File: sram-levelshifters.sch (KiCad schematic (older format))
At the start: 16 parts, among them U10 TXB0108-PW, U11 ISSI61WV5128BL, U12 ISSI61WV5128BL, U13 ISSI61WV5128BL, U14 ISSI61WV5128BL, U2 74HC04, U4 TXB0108-PW, U5 TXB0108-PW, U6 TXB0108-PW, U7 74HC04, U8 TXB0108-PW, U9 74HC04

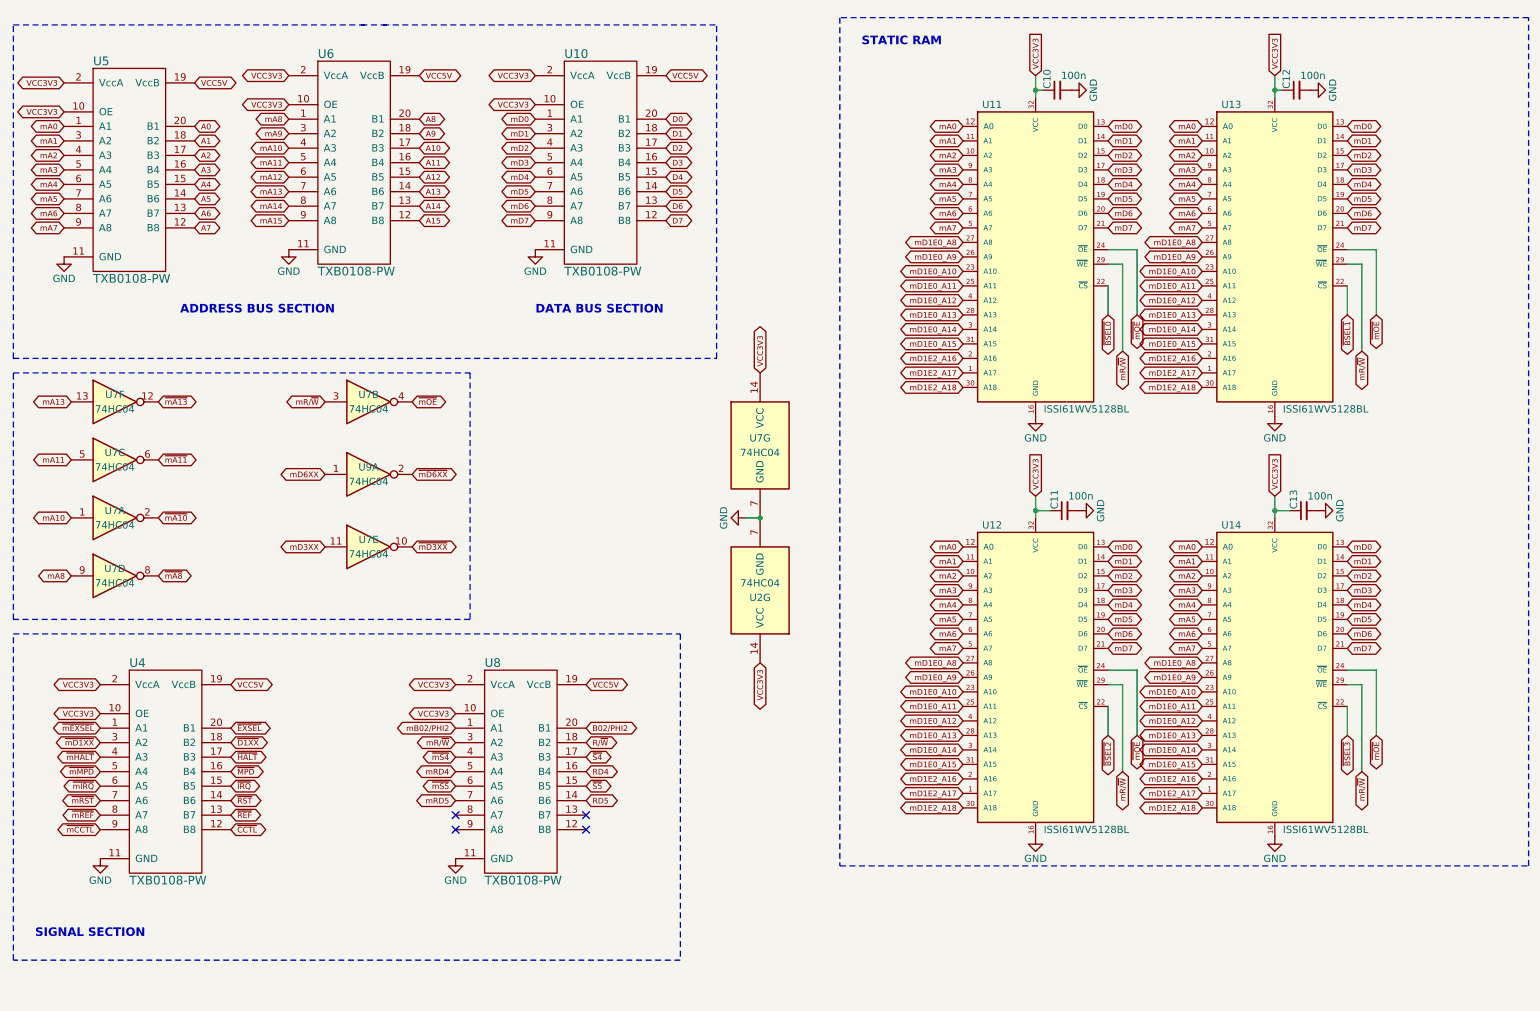
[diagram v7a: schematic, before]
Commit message: Heavily modified. Now it sports a 1024/2048k MIO Ram Expansion and a UNO Cart
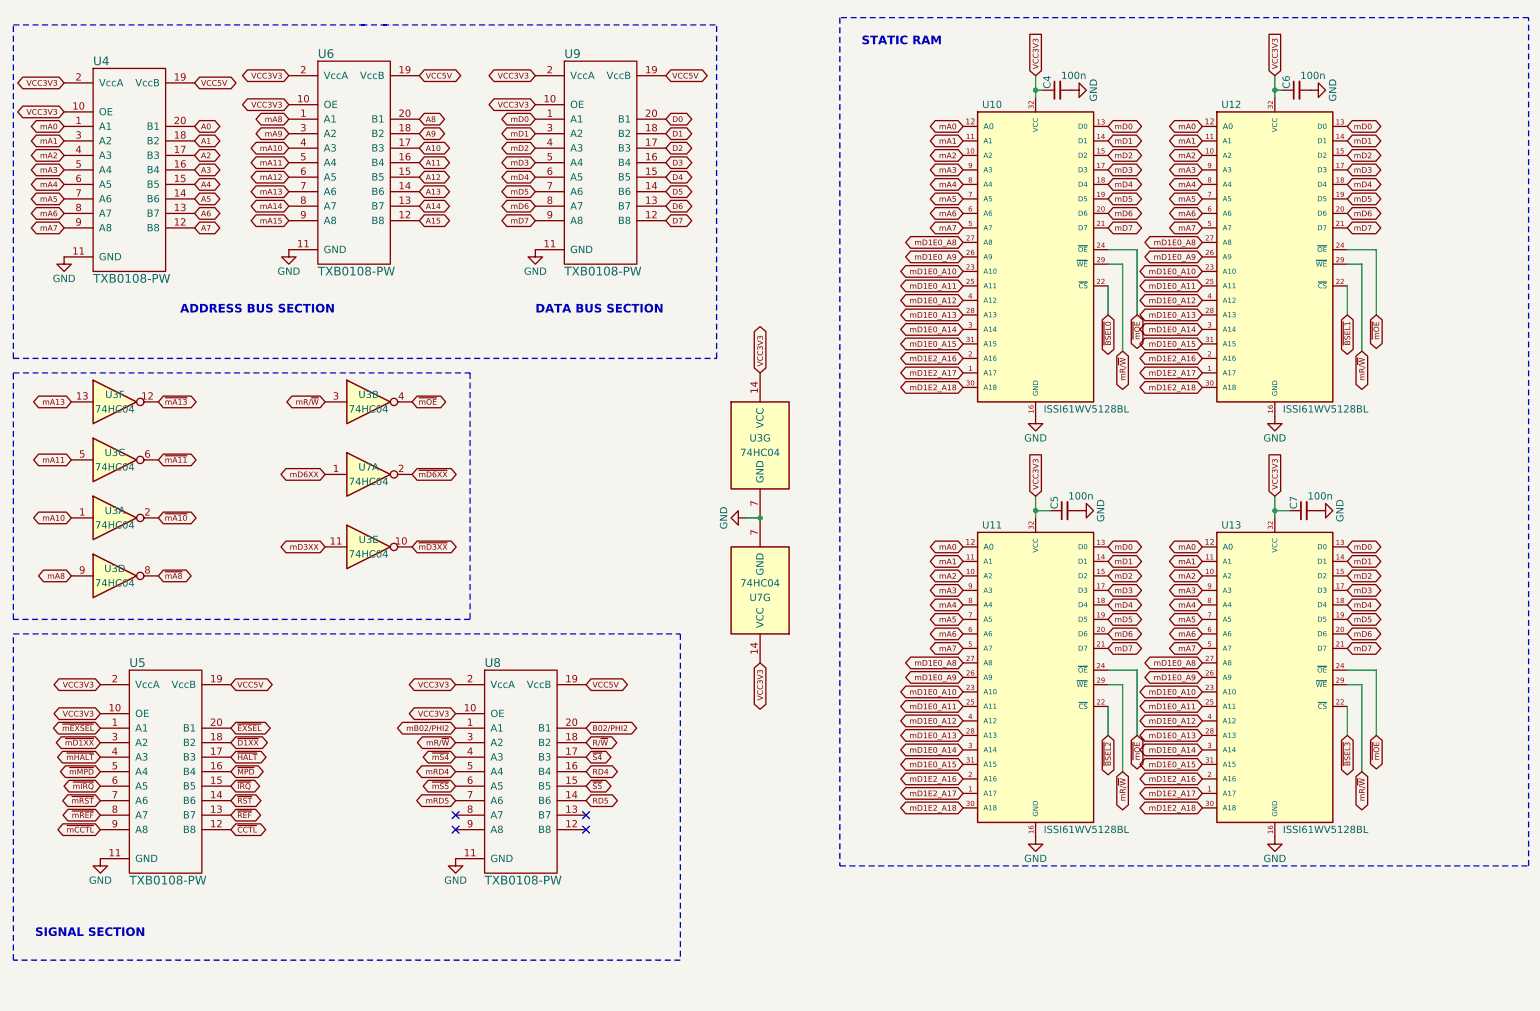
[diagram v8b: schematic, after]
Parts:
- renumbered C10 to C4, C11 to C5, C12 to C6, C13 to C7, U11 to U10, U12 to U11, U13 to U12, U14 to U13, U7 to U3, U5 to U4, U4 to U5, U2 to U7, U9 to U7, U10 to U9
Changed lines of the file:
@@
 $EndDescr
 $Comp
-L ISSI61WV5128BL U11
+L ISSI61WV5128BL U10
 U 1 1 5C2B9006
 P 7650 2250
-F 0 "U11" H 7350 3300 50  0000 C CNN
+F 0 "U10" H 7350 3300 50  0000 C CNN
 F 1 "ISSI61WV5128BL" H 8000 1200 50  0000 C CNN
 F 2 "RetroBitLab:SOP-32L-20.5x11.30-1.27mm" H 7650 2250 50  0001 C CIN
@@
 	7650 1000 7650 1150
 $Comp
-L C_Small C10
+L C_Small C4
 U 1 1 5C2BF542
 P 7800 1100
-F 0 "C10" H 7810 1170 50  0000 L CNN
+F 0 "C4" H 7810 1170 50  0000 L CNN
 F 1 "100n" V 7900 900 50  0000 L CNN
 F 2 "Capacitors_SMD:C_1206_HandSoldering" H 7800 1100 50  0001 C CNN
@@
 $EndComp
 $Comp
-L TXB0108-PW U5
+L TXB0108-PW U4
 U 1 1 5C2BF846
 P 1350 1650
-F 0 "U5" H 1150 2400 60  0000 L CNN
+F 0 "U4" H 1150 2400 60  0000 L CNN
 F 1 "TXB0108-PW" H 1150 900 60  0000 L CNN
 F 2 "Housings_SSOP:SSOP-20_4.4x6.5mm_Pitch0.65mm" H 1150 1600 60  0001 C CNN
@@
 $EndComp
 $Comp
-L TXB0108-PW U4
+L TXB0108-PW U5
 U 1 1 5C2BF9CC
 P 1600 5800
-F 0 "U4" H 1400 6550 60  0000 L CNN
+F 0 "U5" H 1400 6550 60  0000 L CNN
 F 1 "TXB0108-PW" H 1400 5050 60  0000 L CNN
 F 2 "Housings_SSOP:SSOP-20_4.4x6.5mm_Pitch0.65mm" H 1400 5750 60  0001 C CNN
@@
 $EndComp
 $Comp
-L TXB0108-PW U10
+L TXB0108-PW U9
 U 1 1 5C2BFAD5
 P 4600 1600
-F 0 "U10" H 4400 2350 60  0000 L CNN
+F 0 "U9" H 4400 2350 60  0000 L CNN
 F 1 "TXB0108-PW" H 4400 850 60  0000 L CNN
 F 2 "Housings_SSOP:SSOP-20_4.4x6.5mm_Pitch0.65mm" H 4400 1550 60  0001 C CNN
@@
 mD7
 $Comp
-L ISSI61WV5128BL U13
+L ISSI61WV5128BL U12
 U 1 1 5C2DCB84
 P 9300 2250
-F 0 "U13" H 9000 3300 50  0000 C CNN
+F 0 "U12" H 9000 3300 50  0000 C CNN
 F 1 "ISSI61WV5128BL" H 9650 1200 50  0000 C CNN
 F 2 "RetroBitLab:SOP-32L-20.5x11.30-1.27mm" H 9300 2250 50  0001 C CIN
@@
 	9300 1000 9300 1150
 $Comp
-L C_Small C12
+L C_Small C6
 U 1 1 5C2DCB9F
 P 9450 1100
-F 0 "C12" H 9460 1170 50  0000 L CNN
+F 0 "C6" H 9460 1170 50  0000 L CNN
 F 1 "100n" V 9550 900 50  0000 L CNN
 F 2 "Capacitors_SMD:C_1206_HandSoldering" H 9450 1100 50  0001 C CNN
@@
 mD7
 $Comp
-L ISSI61WV5128BL U12
+L ISSI61WV5128BL U11
 U 1 1 5C2DCEF9
 P 7650 5150
-F 0 "U12" H 7350 6200 50  0000 C CNN
+F 0 "U11" H 7350 6200 50  0000 C CNN
 F 1 "ISSI61WV5128BL" H 8000 4100 50  0000 C CNN
 F 2 "RetroBitLab:SOP-32L-20.5x11.30-1.27mm" H 7650 5150 50  0001 C CIN
@@
 	7650 3900 7650 4050
 $Comp
-L C_Small C11
+L C_Small C5
 U 1 1 5C2DCF14
 P 7850 4000
-F 0 "C11" H 7860 4070 50  0000 L CNN
+F 0 "C5" H 7860 4070 50  0000 L CNN
 F 1 "100n" V 7950 3800 50  0000 L CNN
 F 2 "Capacitors_SMD:C_1206_HandSoldering" H 7850 4000 50  0001 C CNN
@@
 mD7
 $Comp
-L ISSI61WV5128BL U14
+L ISSI61WV5128BL U13
 U 1 1 5C2DCF3B
 P 9300 5150
-F 0 "U14" H 9000 6200 50  0000 C CNN
+F 0 "U13" H 9000 6200 50  0000 C CNN
 F 1 "ISSI61WV5128BL" H 9650 4100 50  0000 C CNN
 F 2 "RetroBitLab:SOP-32L-20.5x11.30-1.27mm" H 9300 5150 50  0001 C CIN
@@
 	9300 3900 9300 4050
 $Comp
-L C_Small C13
+L C_Small C7
 U 1 1 5C2DCF56
 P 9500 4000
-F 0 "C13" H 9510 4070 50  0000 L CNN
+F 0 "C7" H 9510 4070 50  0000 L CNN
 F 1 "100n" V 9600 3800 50  0000 L CNN
 F 2 "Capacitors_SMD:C_1206_HandSoldering" H 9500 4000 50  0001 C CNN
@@
 mA10
 $Comp
-L 74HC04 U7
+L 74HC04 U3
 U 2 1 5C2DFEE1
 P 3050 3250
-F 0 "U7" H 3050 3300 50  0000 C CNN
+F 0 "U3" H 3050 3300 50  0000 C CNN
 F 1 "74HC04" H 3050 3200 50  0000 C CNN
 F 2 "Housings_SSOP:TSSOP-14_4.4x5mm_Pitch0.65mm" H 3050 3250 50  0001 C CNN
@@
 $EndComp
 $Comp
-L 74HC04 U7
+L 74HC04 U3
 U 3 1 5C2DFF28
 P 1300 3650
-F 0 "U7" H 1300 3700 50  0000 C CNN
+F 0 "U3" H 1300 3700 50  0000 C CNN
 F 1 "74HC04" H 1300 3600 50  0000 C CNN
 F 2 "Housings_SSOP:TSSOP-14_4.4x5mm_Pitch0.65mm" H 1300 3650 50  0001 C CNN
@@
 $EndComp
 $Comp
-L 74HC04 U7
+L 74HC04 U3
 U 4 1 5C2E0001
 P 1300 4450
-F 0 "U7" H 1300 4500 50  0000 C CNN
+F 0 "U3" H 1300 4500 50  0000 C CNN
 F 1 "74HC04" H 1300 4400 50  0000 C CNN
 F 2 "Housings_SSOP:TSSOP-14_4.4x5mm_Pitch0.65mm" H 1300 4450 50  0001 C CNN
@@
 $EndComp
 $Comp
-L 74HC04 U7
+L 74HC04 U3
 U 5 1 5C2E0114
 P 3050 4250
-F 0 "U7" H 3050 4300 50  0000 C CNN
+F 0 "U3" H 3050 4300 50  0000 C CNN
 F 1 "74HC04" H 3050 4200 50  0000 C CNN
 F 2 "Housings_SSOP:TSSOP-14_4.4x5mm_Pitch0.65mm" H 3050 4250 50  0001 C CNN
@@
 $EndComp
 $Comp
-L 74HC04 U7
+L 74HC04 U3
 U 6 1 5C2E0161
 P 1300 3250
-F 0 "U7" H 1300 3300 50  0000 C CNN
+F 0 "U3" H 1300 3300 50  0000 C CNN
 F 1 "74HC04" H 1300 3200 50  0000 C CNN
 F 2 "Housings_SSOP:TSSOP-14_4.4x5mm_Pitch0.65mm" H 1300 3250 50  0001 C CNN
@@
 $EndComp
 $Comp
-L 74HC04 U7
+L 74HC04 U3
 U 7 1 5C2E0C9C
 P 5750 3550
-F 0 "U7" H 5750 3600 50  0000 C CNN
+F 0 "U3" H 5750 3600 50  0000 C CNN
 F 1 "74HC04" H 5750 3500 50  0000 C CNN
 F 2 "Housings_SSOP:TSSOP-14_4.4x5mm_Pitch0.65mm" H 5750 3550 50  0001 C CNN
@@
 ~mD3XX
 $Comp
-L 74HC04 U7
+L 74HC04 U3
 U 1 1 5C2DFE46
 P 1300 4050
-F 0 "U7" H 1300 4100 50  0000 C CNN
+F 0 "U3" H 1300 4100 50  0000 C CNN
 F 1 "74HC04" H 1300 4000 50  0000 C CNN
 F 2 "Housings_SSOP:TSSOP-14_4.4x5mm_Pitch0.65mm" H 1300 4050 50  0001 C CNN
@@
 ~mA10
 $Comp
-L 74HC04 U2
+L 74HC04 U7
 U 7 1 5C420D5D
 P 5750 4550
-F 0 "U2" H 5750 4600 50  0000 C CNN
+F 0 "U7" H 5750 4600 50  0000 C CNN
 F 1 "74HC04" H 5750 4500 50  0000 C CNN
 F 2 "Housings_SSOP:TSSOP-14_4.4x5mm_Pitch0.65mm" H 5750 4550 50  0001 C CNN
@@
 ~mD6XX
 $Comp
-L 74HC04 U9
+L 74HC04 U7
 U 1 1 5C4210C2
 P 3050 3750
-F 0 "U9" H 3050 3800 50  0000 C CNN
+F 0 "U7" H 3050 3800 50  0000 C CNN
 F 1 "74HC04" H 3050 3700 50  0000 C CNN
 F 2 "Housings_SSOP:TSSOP-14_4.4x5mm_Pitch0.65mm" H 3050 3750 50  0001 C CNN
